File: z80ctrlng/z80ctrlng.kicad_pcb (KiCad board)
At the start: 4 copper layers, 101.6 x 53.3 mm, 58 parts, among them J1 RCBus-80, J10 RX_LINK, J11 U254-051T-4BH81-S2S, J2 3V_LINK, J3 TX_LINK, J4 DEBUG, J5 XKTF-0803-0, J6 UEXT, J7 UXCS, J9 SM04B-SRSS-TB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

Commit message: More final touches o.O
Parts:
- removed J7: UXCS, Connector_PinHeader_2.54mm:PinHeader_2x04_P2.54mm_Vertical
- removed LOGO3: RCBUS_Logo, My_Components:RCBUS_Logo
- removed R2: 10K, Resistor_SMD:R_0402_1005Metric
- removed R8: 1K, Resistor_SMD:R_0402_1005Metric
- added JP1: AUTORESET, Jumper:SolderJumper-2_P1.3mm_Bridged_Pad1.0x1.5mm, F.Cu at (221.6, 87.6)
- added Q3: BSS138, Package_TO_SOT_SMD:SOT-23, F.Cu at (168.7, 77.9)
- R5: value 100 -> 1K
- moved R4 24.2 mm to (167.6, 75.2), turned to 0 degrees
- moved R5 20.7 mm to (169.7, 75.2)
- moved D1 18.0 mm to (172.0, 76.6), turned to -90 degrees
- moved R14 15.2 mm to (214.1, 90.9), turned to 180 degrees
- moved C10 14.4 mm to (201.4, 93.8), turned to -90 degrees
- moved Q2 13.1 mm to (214.1, 93.4), turned to -90 degrees
- moved C9 11.8 mm to (211.1, 93.8), turned to 90 degrees
- moved R12 10.6 mm to (218.9, 90.9), turned to 180 degrees
- moved D3 10.5 mm to (208.9, 88.3)
- moved U5 8.92 mm to (206.2, 93.8), turned to 90 degrees
- moved C13 8.89 mm to (216.0, 100.3)
- moved C15 8.89 mm to (220.2, 100.5)
- moved NT1 8.89 mm to (216.9, 105.2)
- moved U6 8.89 mm to (217.7, 103.8)
- moved Y1 8.89 mm to (212.7, 102.5)
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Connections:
- C12 pad 2: ~{RESET} -> Net-(JP1-A)
- D2 pad 2: Net-(D2-A) -> Net-(BT1-+)
- J5 pad MP1: unconnected-(J5-PadMP1) -> GND
- J5 pad MP2: unconnected-(J5-PadMP2) -> GND
- J5 pad MP3: unconnected-(J5-PadMP3) -> GND
- J5 pad MP4: unconnected-(J5-PadMP4) -> GND
- J5 pad P2: unconnected-(J5-DAT3/CD-PadP2) -> Net-(J5-DAT3/CD)
- J5 pad P3: ~{SS} -> MOSI
- J5 pad P4: MOSI -> +3.3V
- J5 pad P5: +3.3V -> SCK
- J5 pad P6: SCK -> GND
- J5 pad P7: GND -> MISO
- J5 pad P8: MISO -> unconnected-(J5-DAT1-PadP8)
- J6 pad 10: Net-(J6-Pin_10) -> ~{SS}
- R4 pad 2: ~{SS} -> Net-(J5-DAT3/CD)
- R5 pad 1: ~{SS} -> Net-(J5-DAT3/CD)
- U2 pad 14: /BCK -> ~{SDCS}
- U2 pad 46: CTS -> /BCK
- U7 pad 9: CTS -> unconnected-(U7-~{CTS}-Pad9)
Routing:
- net +3.3V: track 20.1 -> 132.3 mm, vias 10 -> 11
- net +5V: track 24.2 -> 90.6 mm, vias 11 -> 8
- net ~{SDCS}: track 0.00 -> 58.0 mm, vias 0 -> 4
- net CTS: track 51.2 -> 0.00 mm, vias 2 -> 0
- net ~{RESET}: track 183.7 -> 134.2 mm
- net Net-(J6-Pin_10): track 25.2 -> 0.00 mm
- net TX3V: track 95.5 -> 77.8 mm, vias 3 -> 1
- net /BCK: track 33.2 -> 15.7 mm
- net TXU: track 46.7 -> 60.7 mm
- net Net-(J5-DAT3/CD): track 0.00 -> 13.9 mm
- net Net-(D2-K): track 10.8 -> 24.6 mm, vias 0 -> 2
- net RXU: track 49.5 -> 61.9 mm
- net MISO: track 101.4 -> 90.8 mm, vias 3 -> 2
- net Net-(Q2-D): track 14.9 -> 24.3 mm
- net ~{SS}: track 92.4 -> 85.7 mm, vias 3 -> 4
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- added copper zone on B.Cu, net +5V
- added copper zone on In2.Cu, net GND
- added copper zone on In2.Cu, net GND1
- removed copper zone on In2.Cu, net +3.3V
- removed copper zone on In2.Cu, net +5V
- removed copper zone on B.Cu, net GND
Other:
- board text added: "74HCT257"
- board text added: "74HCT541"
- board text added: "AS6C4008"
- board text added: "RCBUS"
- board text removed: "3V3"
- board text removed: "|-UEXT CS-|"

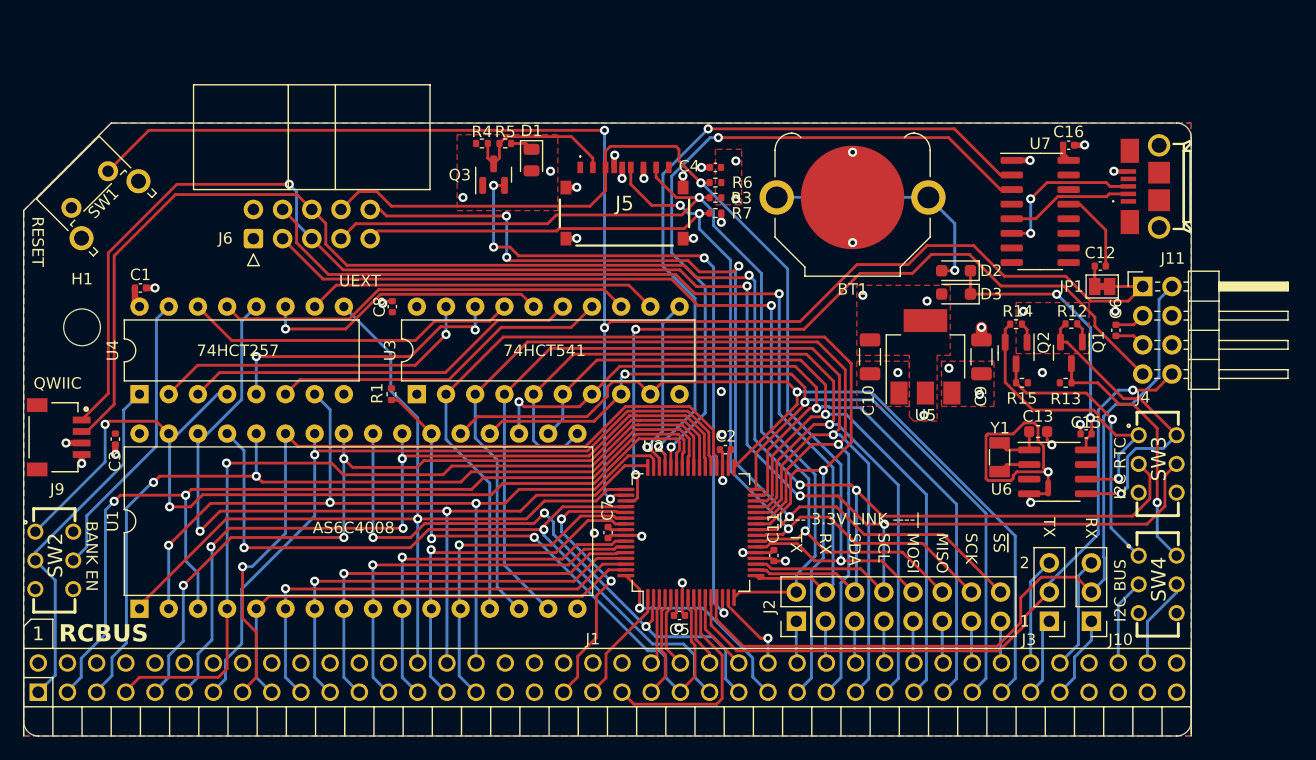
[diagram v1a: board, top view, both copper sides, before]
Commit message: Muntz unnecessary jumpers/switches; add SerialUDPI programmer; cleanup layout
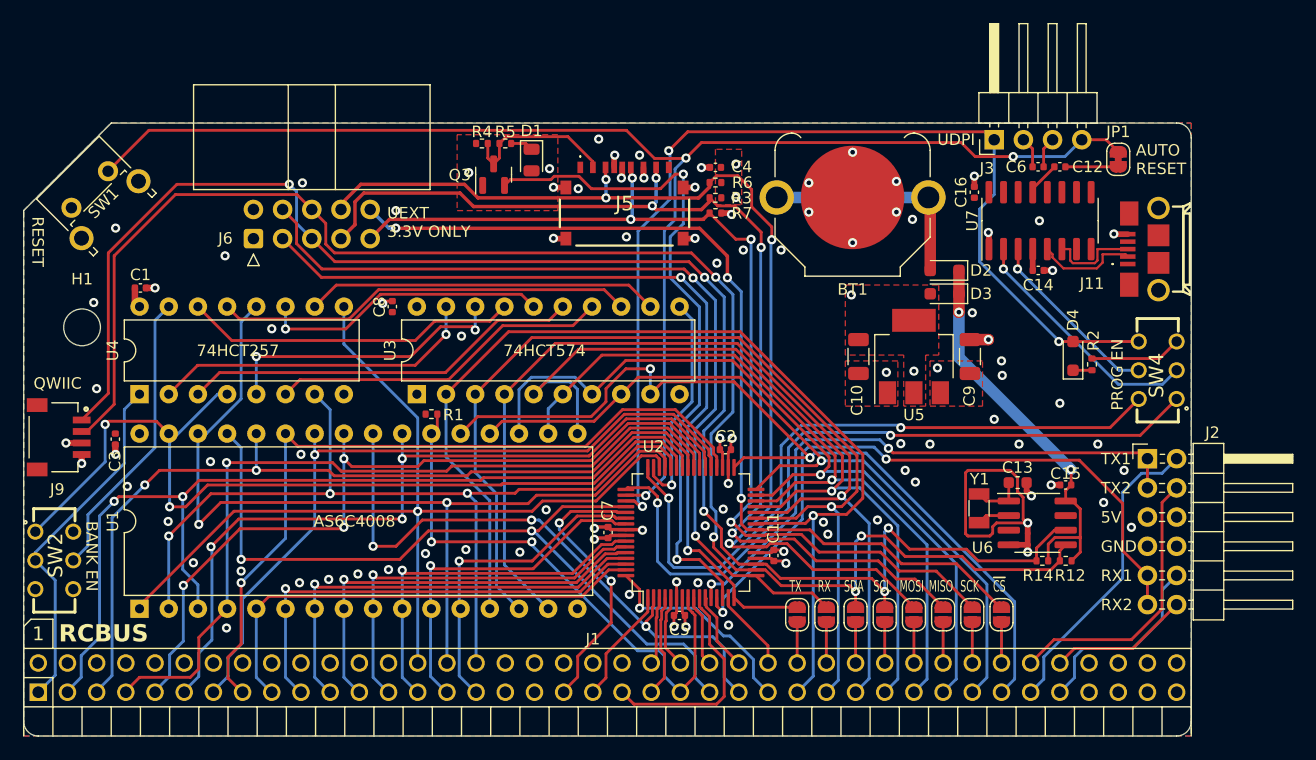
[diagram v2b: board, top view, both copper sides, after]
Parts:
- removed J10: RX_LINK, Connector_PinHeader_2.54mm:PinHeader_1x03_P2.54mm_Vertical
- removed J4: DEBUG, Connector_PinHeader_2.54mm:PinHeader_2x04_P2.54mm_Horizontal
- removed Q1, Q2: BSS138, Package_TO_SOT_SMD:SOT-23
- removed R13, R15: 4.7K, Resistor_SMD:R_0402_1005Metric
- removed SW3: RTC, SamacSys_Parts:JS202011CQN
- added C14: 0.1uf, Capacitor_SMD:C_0402_1005Metric, F.Cu at (216.0, 86.2)
- added D4: 1N5819WS, Diode_SMD:D_SOD-323_HandSoldering, F.Cu at (219.1, 93.7)
- added JP10: SCK, Jumper:SolderJumper-2_P1.3mm_Open_RoundedPad1.0x1.5mm, F.Cu at (210.3, 116.2)
- added JP11: CS, Jumper:SolderJumper-2_P1.3mm_Open_RoundedPad1.0x1.5mm, F.Cu at (212.9, 116.2)
- added JP2: TX3V, Jumper:SolderJumper-2_P1.3mm_Open_RoundedPad1.0x1.5mm, F.Cu at (195.1, 116.2)
- added JP3: RX3V, Jumper:SolderJumper-2_P1.3mm_Open_RoundedPad1.0x1.5mm, F.Cu at (197.6, 116.2)
- added JP6: SDA, Jumper:SolderJumper-2_P1.3mm_Open_RoundedPad1.0x1.5mm, F.Cu at (200.2, 116.2)
- added JP7: SCL, Jumper:SolderJumper-2_P1.3mm_Open_RoundedPad1.0x1.5mm, F.Cu at (202.7, 116.2)
- added JP8: MOSI, Jumper:SolderJumper-2_P1.3mm_Open_RoundedPad1.0x1.5mm, F.Cu at (205.2, 116.2)
- added JP9: MISO, Jumper:SolderJumper-2_P1.3mm_Open_RoundedPad1.0x1.5mm, F.Cu at (207.8, 116.2)
- added R2: 4.7K, Resistor_SMD:R_0402_1005Metric, F.Cu at (220.7, 94.4)
- J2: value 3V_LINK -> SERIAL; footprint Connector_PinHeader_2.54mm:PinHeader_2x08_P2.54mm_Vertical -> Connector_PinHeader_2.54mm:PinHeader_2x06_P2.54mm_Horizontal
- J3: value TX_LINK -> UDPI; footprint Connector_PinHeader_2.54mm:PinHeader_1x03_P2.54mm_Vertical -> Connector_PinHeader_2.54mm:PinHeader_1x04_P2.54mm_Horizontal
- JP1: footprint Jumper:SolderJumper-2_P1.3mm_Bridged_Pad1.0x1.5mm -> Jumper:SolderJumper-2_P1.3mm_Bridged_RoundedPad1.0x1.5mm
- SW4: value BUS -> PROG_EN
- moved J3 42.2 mm to (212.2, 74.9), turned to 90 degrees
- moved J2 33.7 mm to (225.6, 102.6), turned to 0 degrees
- moved R14 20.7 mm to (216.4, 111.5)
- moved R12 20.6 mm to (218.4, 111.5)
- moved SW4 18.6 mm to (226.4, 94.9), turned to 90 degrees
- moved C6 15.8 mm to (216.0, 77.2), turned to 180 degrees
- moved JP1 11.2 mm to (223.0, 76.6), turned to 90 degrees
- moved C12 9.32 mm to (217.9, 77.2), turned to 0 degrees
- moved C16 9.17 mm to (210.5, 79.4), turned to 90 degrees
- moved J11 5.45 mm to (226.2, 84.4)
- moved C15 4.79 mm to (218.4, 104.9)
- moved C13 4.79 mm to (214.3, 104.7)
- moved NT1 4.79 mm to (215.1, 109.6)
- moved Y1 4.79 mm to (210.9, 106.9)
- moved U6 4.79 mm to (216.0, 108.2)
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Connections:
- net Net-(J11-D+) renamed /Peripherals/UD+
- net Net-(J11-D-) renamed /Peripherals/UD-
- C6 pad 1: +5V -> GND
- C6 pad 2: GND -> +5V
- J1 pad 40: unconnected-(J1-Pin_40-Pad40) -> /USER4
- J1 pad 78: SCL5V -> /USER6
- J1 pad 79: SDA5V -> /USER7
- J1 pad 80: unconnected-(J1-Pin_80-Pad80) -> /USER8
- J2 pad 1: /D8 -> TXB
- J2 pad 10: MOSI -> /RX1B
- J2 pad 11: /D13 -> RXB
- J2 pad 12: MISO -> /RX2B
- J2 pad 2: TX3V -> /TX1B
- J2 pad 3: /D9 -> TXB
- J2 pad 4: RX3V -> /TX2B
- J2 pad 5: /D10 -> +5V
- J2 pad 6: SDA -> +5V
- J2 pad 7: /D11 -> GND
- J2 pad 8: SCL -> GND
- J2 pad 9: /D12 -> RXB
- J3 pad 1: /TX1B -> UPDI
- J3 pad 2: TXB -> +5V
- J3 pad 3: /TX2B -> GND
- J6 pad 10: ~{SS} -> ~{CS}
- J6 pad 3: TX3V -> TXC
- J6 pad 4: RX3V -> RXC
- R12 pad 1: +3.3V -> Net-(D2-K)
- R12 pad 2: Net-(Q1-S) -> SDA
- R14 pad 1: +3.3V -> Net-(D2-K)
- R14 pad 2: Net-(Q2-S) -> SCL
- SW4 pad 1: Net-(Q2-D) -> RXF
- SW4 pad 2: SCL5V -> /Peripherals/USBTX
- SW4 pad 3: unconnected-(SW4-Pad3) -> Net-(SW4A-C)
- SW4 pad 4: Net-(Q1-D) -> TXF
- SW4 pad 5: SDA5V -> /Peripherals/USBRX
- SW4 pad 6: unconnected-(SW4-Pad6) -> UPDI
- U2 pad 16: TX3V -> TXC
- U2 pad 17: RX3V -> RXC
- U2 pad 25: ~{SS} -> ~{CS}
- U2 pad 44: TXU -> /A16
- U2 pad 45: RXU -> /A17
- U2 pad 46: /BCK -> /A18
- U2 pad 47: /A16 -> /BCK
- U2 pad 48: /A17 -> TXF
- U2 pad 49: /A18 -> RXF
- U2 pad 51: Net-(J4-Pin_7) -> UPDI
- U6 pad 5: Net-(Q1-S) -> SDA
- U6 pad 6: Net-(Q2-S) -> SCL
- U7 pad 2: RXU -> /Peripherals/USBTX
- U7 pad 3: TXU -> /Peripherals/USBRX
- U7 pad 4: unconnected-(U7-V3-Pad4) -> Net-(U7-V3)
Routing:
- net UPDI: track 0.00 -> 91.1 mm, vias 0 -> 3
- net ~{SS}: track 85.7 -> 0.00 mm, vias 4 -> 0
- net ~{CS}: track 0.00 -> 82.1 mm, vias 0 -> 3
- net RX3V: track 82.0 -> 0.00 mm, vias 1 -> 0
- net TX3V: track 77.8 -> 0.00 mm, vias 1 -> 0
- net RXC: track 0.00 -> 77.3 mm, vias 0 -> 2
- net TXC: track 0.00 -> 73.6 mm, vias 0 -> 2
- net Net-(J4-Pin_7): track 67.6 -> 0.00 mm, vias 2 -> 0
- net RXF: track 0.00 -> 64.0 mm, vias 0 -> 2
- net RXU: track 61.9 -> 0.00 mm, vias 2 -> 0
- net TXU: track 60.7 -> 0.00 mm, vias 2 -> 0
- net TXF: track 0.00 -> 59.4 mm, vias 0 -> 2
- net +5V: track 90.6 -> 48.1 mm, vias 8 -> 9
- net Net-(Q1-S): track 26.8 -> 0.00 mm, vias 1 -> 0
- net Net-(Q2-S): track 26.3 -> 0.00 mm, vias 1 -> 0
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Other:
- board text added: "74HCT574"
- board text added: "AUTO RESET"
- board text added: "PROG EN"
- board text added: "RX1"
- board text added: "RX2"
- board text added: "TX1"
- board text added: "TX2"
- board text added: "UDPI"
- board text added: "UEXT 3.3V ONLY"
- board text added: "~{CS}"
- board text removed: "1"
- board text removed: "2"
- board text removed: "74HCT541"
- board text removed: "I2C BUS"
- board text removed: "I2C RTC"
- board text removed: "RST"
- board text removed: "UEXT"
- board text removed: "UPDI"
- board text removed: "|---- 3.3V LINK ----|"
- board text removed: "~{SS}"

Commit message: Rearrange to make fast 3.3V buses shorter
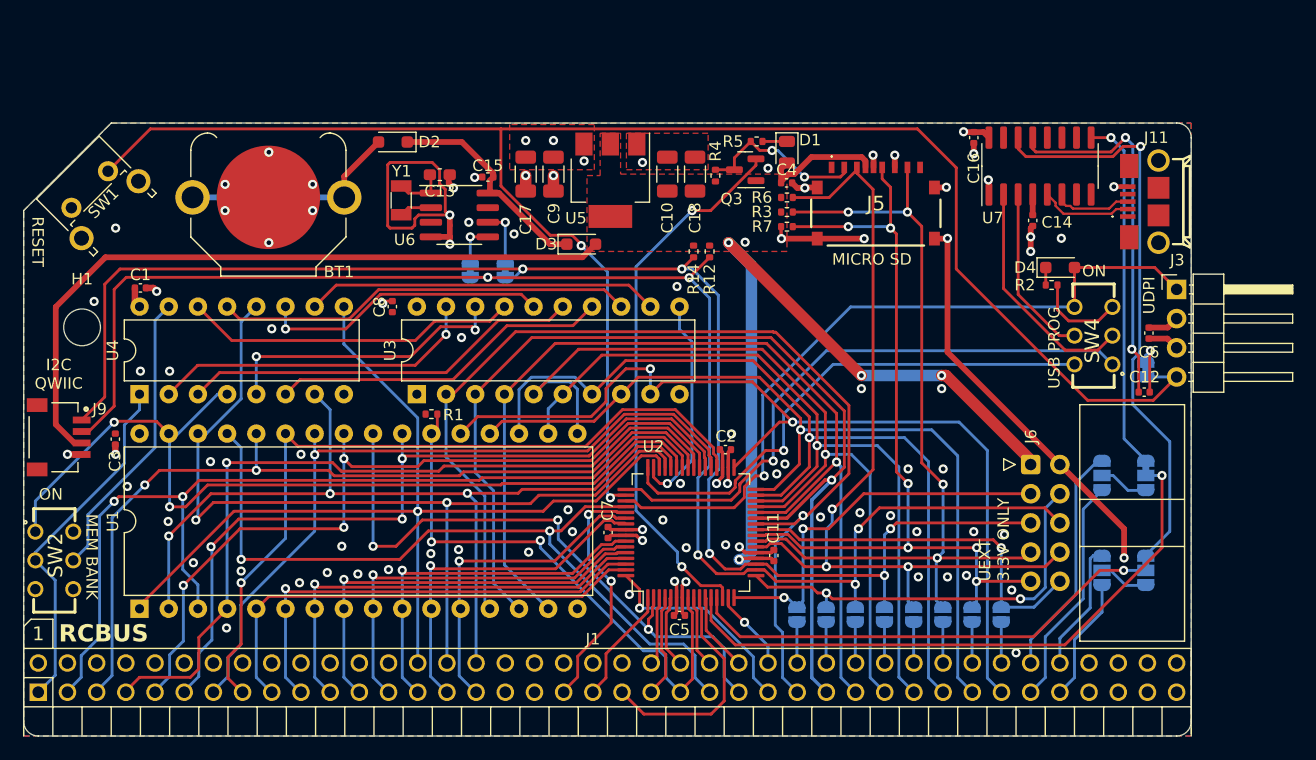
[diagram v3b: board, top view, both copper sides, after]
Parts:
- removed J2: SERIAL, Connector_PinHeader_2.54mm:PinHeader_2x06_P2.54mm_Horizontal
- added C17: 22uf, Capacitor_SMD:C_1206_3216Metric, F.Cu at (171.4, 77.9)
- added C18: 22uf, Capacitor_SMD:C_1206_3216Metric, F.Cu at (186.2, 77.9)
- added JP12: RXB, Jumper:SolderJumper-3_P1.3mm_Open_RoundedPad1.0x1.5mm, B.Cu at (221.6, 112.3)
- added JP13: RTC_SCL, Jumper:SolderJumper-2_P1.3mm_Bridged_RoundedPad1.0x1.5mm, B.Cu at (169.7, 86.2)
- added JP14: CTS, Jumper:SolderJumper-3_P1.3mm_Bridged12_RoundedPad1.0x1.5mm, B.Cu at (225.4, 104.1)
- added JP15: RTC_SDA, Jumper:SolderJumper-2_P1.3mm_Bridged_RoundedPad1.0x1.5mm, B.Cu at (166.6, 86.2)
- added JP4: TXB, Jumper:SolderJumper-3_P1.3mm_Open_RoundedPad1.0x1.5mm, B.Cu at (221.6, 104.1)
- added JP5: RTS, Jumper:SolderJumper-3_P1.3mm_Bridged12_RoundedPad1.0x1.5mm, B.Cu at (225.4, 112.3)
- C13: footprint Capacitor_SMD:C_0603_1608Metric -> Capacitor_SMD:C_0603_1608Metric_Pad1.08x0.95mm_HandSolder
- J1: value RCBus-80 -> RCBUS
- JP1, JP10, JP11, JP2, JP3, JP6, JP7, JP8, JP9: moved to B.Cu
- R12, R14: value 4.7K -> 2.2K
- moved J6 70.4 mm to (215.4, 103.1), turned to 0 degrees
- moved C15 57.0 mm to (168.1, 78.1)
- moved U6 57.0 mm to (165.7, 81.4)
- moved C13 57.0 mm to (164.0, 77.9)
- moved NT1 57.0 mm to (164.8, 82.8)
- moved Y1 57.0 mm to (160.6, 80.1)
- moved BT1 50.8 mm to (149.1, 79.9)
- moved D2 49.3 mm to (159.9, 75.1)
- moved R12 41.0 mm to (187.5, 84.6), turned to -90 degrees
- moved R14 40.6 mm to (186.1, 84.6), turned to -90 degrees
- moved C9 39.6 mm to (173.9, 77.9), turned to -90 degrees
- moved D3 31.9 mm to (176.3, 83.9), turned to 0 degrees
- moved U5 30.5 mm to (178.8, 78.4), turned to -90 degrees
- moved C10 23.0 mm to (183.8, 77.9), turned to 90 degrees
- moved D1 22.2 mm to (194.2, 75.9)
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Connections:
- net RXF renamed PF5
- net TXF renamed PF4
- R12 pad 1: Net-(D2-K) -> +3.3V
- R14 pad 1: Net-(D2-K) -> +3.3V
- U2 pad 12: TXB -> PB4
- U2 pad 13: RXB -> PB5
- U6 pad 5: SDA -> Net-(JP15-B)
- U6 pad 6: SCL -> Net-(JP13-B)
- U7 pad 14: unconnected-(U7-~{RTS}-Pad14) -> ~{RTS}
- U7 pad 9: unconnected-(U7-~{CTS}-Pad9) -> ~{CTS}
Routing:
- net RXB: track 58.1 -> 0.00 mm, vias 2 -> 0
- net PB4: track 0.00 -> 53.3 mm, vias 0 -> 1
- net TXB: track 50.8 -> 0.00 mm, vias 2 -> 0
- net ~{RTS}: track 0.00 -> 50.3 mm, vias 0 -> 1
- net ~{CS}: track 82.1 -> 33.2 mm, vias 3 -> 1
- net GND: track 33.7 -> 80.3 mm, vias 80 -> 78
- net PB5: track 0.00 -> 41.9 mm, vias 0 -> 1
- net RXC: track 77.3 -> 36.4 mm
- net TXC: track 73.6 -> 33.9 mm
- net +5V: track 48.1 -> 16.3 mm, vias 9 -> 13
- net ~{CTS}: track 0.00 -> 31.1 mm, vias 0 -> 1
- net Net-(U7-~{DTR}): track 2.99 -> 32.4 mm, vias 0 -> 2
- net UPDI: track 91.1 -> 64.5 mm, vias 3 -> 1
- net ~{RESET}: track 125.1 -> 151.6 mm, vias 3 -> 2
- net MISO: track 93.8 -> 74.9 mm
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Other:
- board text added: "512KB SRAM AS6C4008"
- board text added: "BANK MULTIPLEXER 74HCT257"
- board text added: "BANK REGISTER 74HCT574"
- board text added: "I2C QWIIC"
- board text added: "MEM BANK"
- board text added: "MICRO SD"
- board text added: "ON"
- board text added: "PB4"
- board text added: "PB5"
- board text added: "RTC"
- board text added: "RXB"
- board text added: "TXB"
- board text added: "USB PROG"
- board text added: "___ ___ _ _ ___( _ ) / _ \ ___| |_ _ __| | |_ / _ \| | | |/ __| __| '__| | / / (_) | |_| | (__| |_| | | | /___\___/ \___/ \___|\__|_| |_|"
- board text added: "z80ctrl NG REV1 © 2023 J.B. Langston https://github.com/jblang/z80ctrl"
- board text added: "~{CTS}"
- board text added: "~{DTR}"
- board text added: "~{RESET}"
- board text added: "~{RTS}"
- board text removed: "512KB SRAM"
- board text removed: "5V"
- board text removed: "74HCT257"
- board text removed: "74HCT574"
- board text removed: "AS6C4008"
- board text removed: "AUTO RESET"
- board text removed: "BANK EN"
- board text removed: "BANK MULTIPLEXER"
- board text removed: "BANK REGISTER"
- board text removed: "GND"
- board text removed: "PROG EN"
- board text removed: "QWIIC"
- board text removed: "___ ___ _ _ ___( _ ) / _ \ ___| |_ _ __| | |_ / _ \| | | |/ __| __| '__| | / / (_) | |_| | (__| |_| | | | /___\___/ \___/ \___|\__|_| |_| z80ctrl NG REV1 (C)2023 J.B. Langston https://github.com/jblang/z80ctrl"

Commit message: Copper pour, via stitching, silkscreen
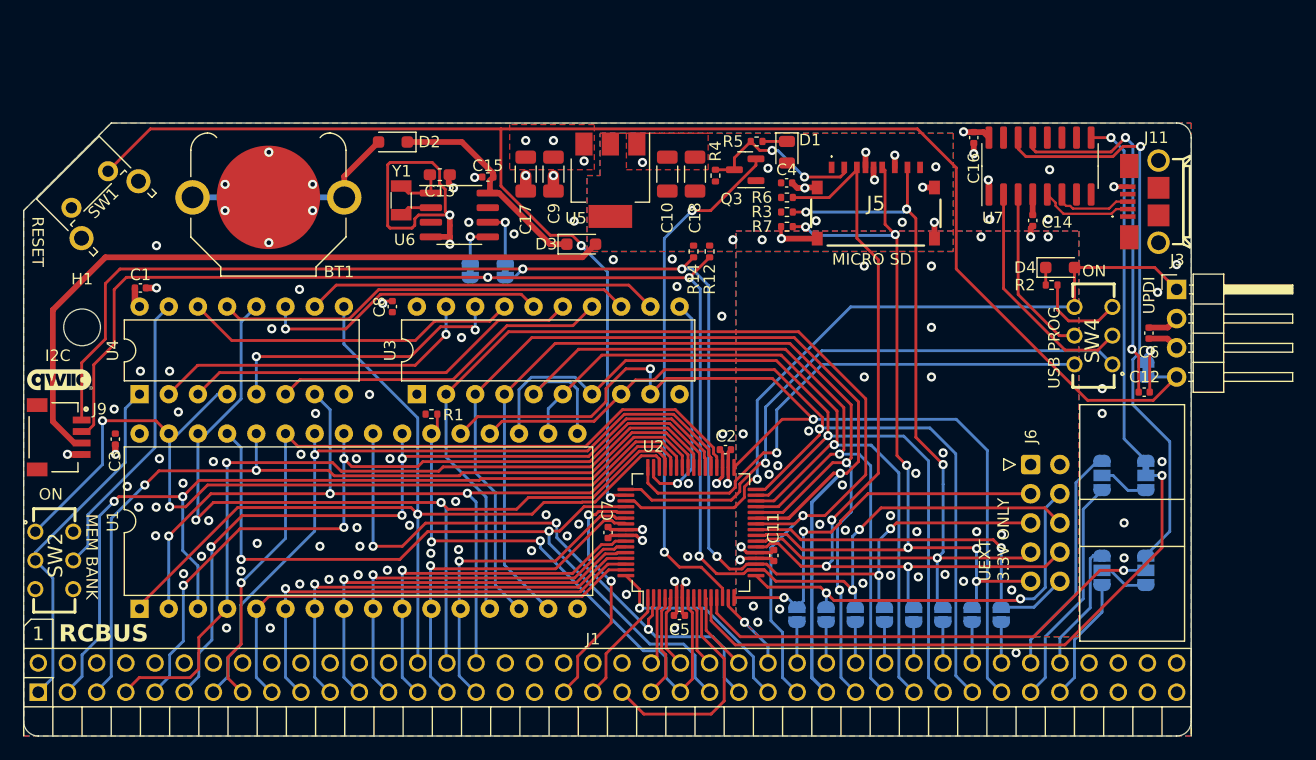
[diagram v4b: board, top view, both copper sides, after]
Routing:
- net +3.3V: track 140.5 -> 67.4 mm, vias 4 -> 14
- net GND: track 80.3 -> 40.8 mm, vias 78 -> 90
- net /D0: track 93.2 -> 96.8 mm
- net /D1: track 91.2 -> 94.7 mm
- net /D2: track 87.3 -> 90.6 mm, vias 1 -> 2
- net /D7: track 82.3 -> 84.4 mm
- net ~{SDCS}: track 47.6 -> 45.6 mm
- net /D3: track 74.0 -> 75.8 mm
- net /D6: track 75.0 -> 76.3 mm
- net SCL: track 129.7 -> 128.5 mm
- net SCK: track 72.4 -> 73.2 mm
- net SDA: track 134.5 -> 133.7 mm
- net /A15: track 77.9 -> 78.6 mm
- net /D4: track 68.7 -> 69.4 mm
- net /A17: track 79.6 -> 80.1 mm
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- added copper zone on B.Cu, net +3.3V
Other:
- board text added: "CH340C"
- board text added: "CR1216"
- board text added: "I2C"
- board text added: "PCF8563"
- board text added: "UPDI"
- board text removed: "I2C QWIIC"
- board text removed: "RTC"
- board text removed: "UDPI"
